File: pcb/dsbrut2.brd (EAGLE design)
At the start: 51.6 x 38 mm, 14 parts, among them IC1 4175D, IC2 74HC125D, IC3 MEGA8-AI

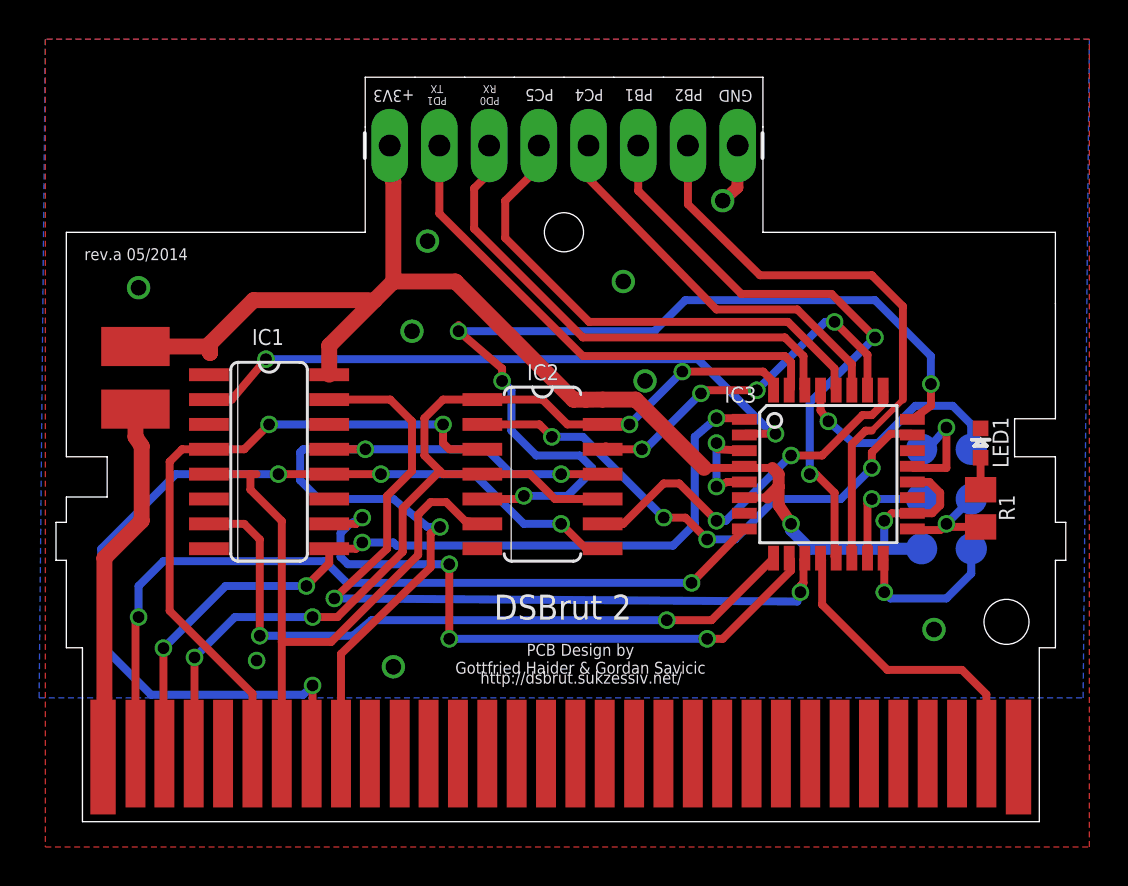
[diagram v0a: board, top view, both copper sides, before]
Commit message: Made pin1 of the ICSP connector square
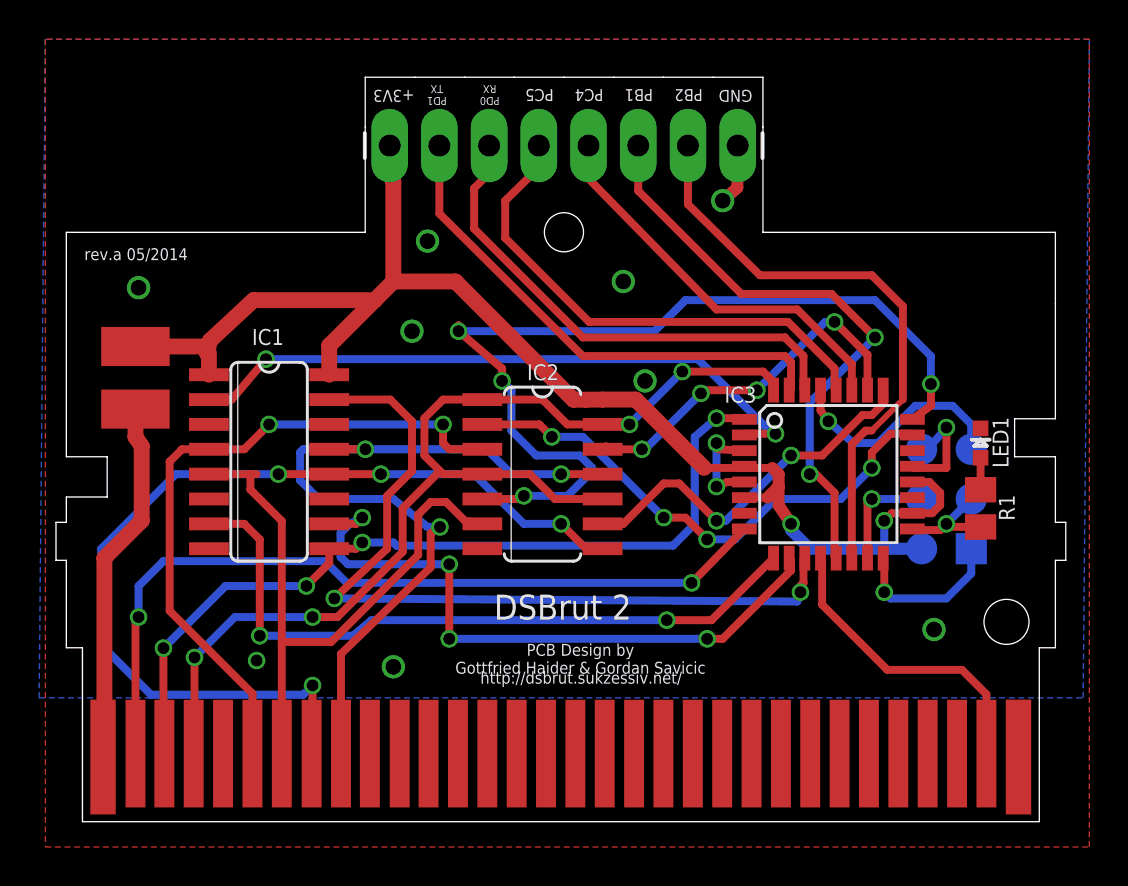
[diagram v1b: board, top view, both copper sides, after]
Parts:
- TP3: value TPSQTP16R -> TPSQTP16SQ; device testpad:TP16R -> testpad:TP16SQ
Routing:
- net +3V3: track 69.8 -> 71.1 mm
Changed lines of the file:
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@@
 <elements>
 <element name="IC1" library="40xx" package="SO16" value="4175D" x="9.525" y="18.415" smashed="yes" rot="R270">
-<attribute name="VALUE" x="8.255" y="17.0815" size="0.8128" layer="27" ratio="10" rot="R270"/>
+<attribute name="VALUE" x="9.525" y="18.3515" size="0.8128" layer="27" ratio="10" rot="R270" align="center"/>
 <attribute name="NAME" x="8.646478125" y="24.380178125" size="0.8128" layer="25" ratio="10"/>
 </element>
 <element name="IC2" library="74xx-eu" package="SO14" value="74HC125D" x="23.495" y="17.78" smashed="yes" rot="R270">
-<attribute name="VALUE" x="28.1305" y="19.05" size="0.8128" layer="27" ratio="10" rot="R270"/>
+<attribute name="VALUE" x="23.0505" y="20.47875" size="0.8128" layer="27" ratio="10" rot="R270" align="center"/>
 <attribute name="NAME" x="22.7028625" y="22.578071875" size="0.8128" layer="25" ratio="10"/>
 </element>
@@
 <attribute name="OC_FARNELL" value="9171371" x="55.88" y="-26.67" size="1.778" layer="27" display="off"/>
 <attribute name="NAME" x="32.7914" y="21.43125" size="0.8128" layer="25"/>
-<attribute name="VALUE" x="37.7825" y="15.0749" size="0.8128" layer="27" rot="R90"/>
+<attribute name="VALUE" x="38.1" y="17.77365" size="0.8128" layer="27" rot="R90" align="center"/>
 </element>
 <element name="U$1" library="nds_cart" package="DS-CARTRIDGE-SLOT2" value="DS_CARTRIDGE_SLOT2" x="0" y="0"/>
 <element name="TP1" library="testpad" package="TP16R" value="TPSQTP16R" x="42.8625" y="13.97" smashed="yes" rot="MR0">
 <attribute name="TP_SIGNAL_NAME" value="" x="42.8625" y="11.43" size="1" layer="38" rot="MR0"/>
-<attribute name="NAME" x="43.6626" y="14.8199" size="0.8128" layer="26" rot="MR0"/>
-<attribute name="VALUE" x="43.4975" y="13.208" size="0.0254" layer="28" rot="MR0"/>
 </element>
 <element name="TP2" library="testpad" package="TP16R" value="TPSQTP16R" x="42.8625" y="16.51" smashed="yes" rot="MR0">
 <attribute name="TP_SIGNAL_NAME" value="" x="42.8625" y="13.97" size="1" layer="38" rot="MR0"/>
-<attribute name="NAME" x="43.6626" y="17.3599" size="0.8128" layer="26" rot="MR0"/>
-<attribute name="VALUE" x="43.4975" y="15.748" size="0.0254" layer="28" rot="MR0"/>
 </element>
-<element name="TP3" library="testpad" package="TP16R" value="TPSQTP16R" x="45.4025" y="13.97" smashed="yes" rot="MR0">
+<element name="TP3" library="testpad" package="TP16SQ" value="TPSQTP16SQ" x="45.4025" y="13.97" smashed="yes" rot="MR0">
 <attribute name="TP_SIGNAL_NAME" value="" x="45.4025" y="11.43" size="1" layer="38" rot="MR0"/>
-<attribute name="NAME" x="46.2026" y="14.8199" size="0.8128" layer="26" rot="MR0"/>
-<attribute name="VALUE" x="46.0375" y="13.208" size="0.0254" layer="28" rot="MR0"/>
 </element>
 <element name="TP4" library="testpad" package="TP16R" value="TPSQTP16R" x="45.4025" y="16.51" smashed="yes" rot="MR0">
 <attribute name="TP_SIGNAL_NAME" value="" x="45.4025" y="13.97" size="1" layer="38" rot="MR0"/>
-<attribute name="NAME" x="46.2026" y="17.3599" size="0.8128" layer="26" rot="MR0"/>
-<attribute name="VALUE" x="46.0375" y="15.748" size="0.0254" layer="28" rot="MR0"/>
 </element>
 <element name="TP5" library="testpad" package="TP16R" value="TPSQTP16R" x="45.4025" y="19.05" smashed="yes" rot="MR0">
 <attribute name="TP_SIGNAL_NAME" value="" x="45.4025" y="16.51" size="1" layer="38" rot="MR0"/>
-<attribute name="NAME" x="46.2026" y="19.8999" size="0.8128" layer="26" rot="MR0"/>
-<attribute name="VALUE" x="46.0375" y="18.288" size="0.0254" layer="28" rot="MR0"/>
 </element>
 <element name="TP6" library="testpad" package="TP16R" value="TPSQTP16R" x="42.8625" y="19.05" smashed="yes" rot="MR0">
 <attribute name="TP_SIGNAL_NAME" value="" x="42.8625" y="16.51" size="1" layer="38" rot="MR0"/>
-<attribute name="NAME" x="43.6626" y="19.8999" size="0.8128" layer="26" rot="MR0"/>
 </element>
 <element name="LED1" library="SparkFunEagle-6-6-07" package="LED-0603" value="" x="45.87875" y="19.3675" smashed="yes">
@@
 <wire x1="43.815" y1="16.8275" x2="43.2625" y2="17.38" width="0.4064" layer="1"/>
 <contactref element="F1" pad="1"/>
-<wire x1="8.73125" y1="26.67" x2="6.50875" y2="24.4475" width="0.8128" layer="1"/>
-<wire x1="6.50875" y1="24.4475" x2="6.50875" y2="23.97125" width="0.8128" layer="1"/>
-<wire x1="6.50875" y1="23.97125" x2="6.50875" y2="22.91715" width="0" layer="19" extent="1-16"/>
-<wire x1="6.50875" y1="22.91715" x2="6.4516" y2="22.86" width="0" layer="19" extent="1-16"/>
+<wire x1="6.50875" y1="24.60625" x2="6.35" y2="23.97125" width="0.8128" layer="1"/>
 <wire x1="2.69875" y1="24.30125" x2="6.3625" y2="24.30125" width="0.8128" layer="1"/>
-<wire x1="6.3625" y1="24.30125" x2="6.50875" y2="23.97125" width="0.8128" layer="1"/>
+<wire x1="6.3625" y1="24.30125" x2="6.35" y2="23.97125" width="0.8128" layer="1"/>
 <contactref element="IC1" pad="16"/>
 <wire x1="12.5984" y1="22.86" x2="12.5984" y2="24.3459" width="0.8128" layer="1"/>
 <wire x1="12.5984" y1="24.3459" x2="14.9225" y2="26.67" width="0.8128" layer="1"/>
+<wire x1="6.35" y1="23.97125" x2="6.4516" y2="23.97125" width="0.4064" layer="1"/>
+<wire x1="6.4516" y1="23.97125" x2="6.4516" y2="22.86" width="0.8128" layer="1"/>
+<wire x1="8.73125" y1="26.67" x2="6.50875" y2="24.60625" width="0.8128" layer="1"/>
 </signal>
 <signal name="PD1">

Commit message: added crystal, jumper bridge for gba2
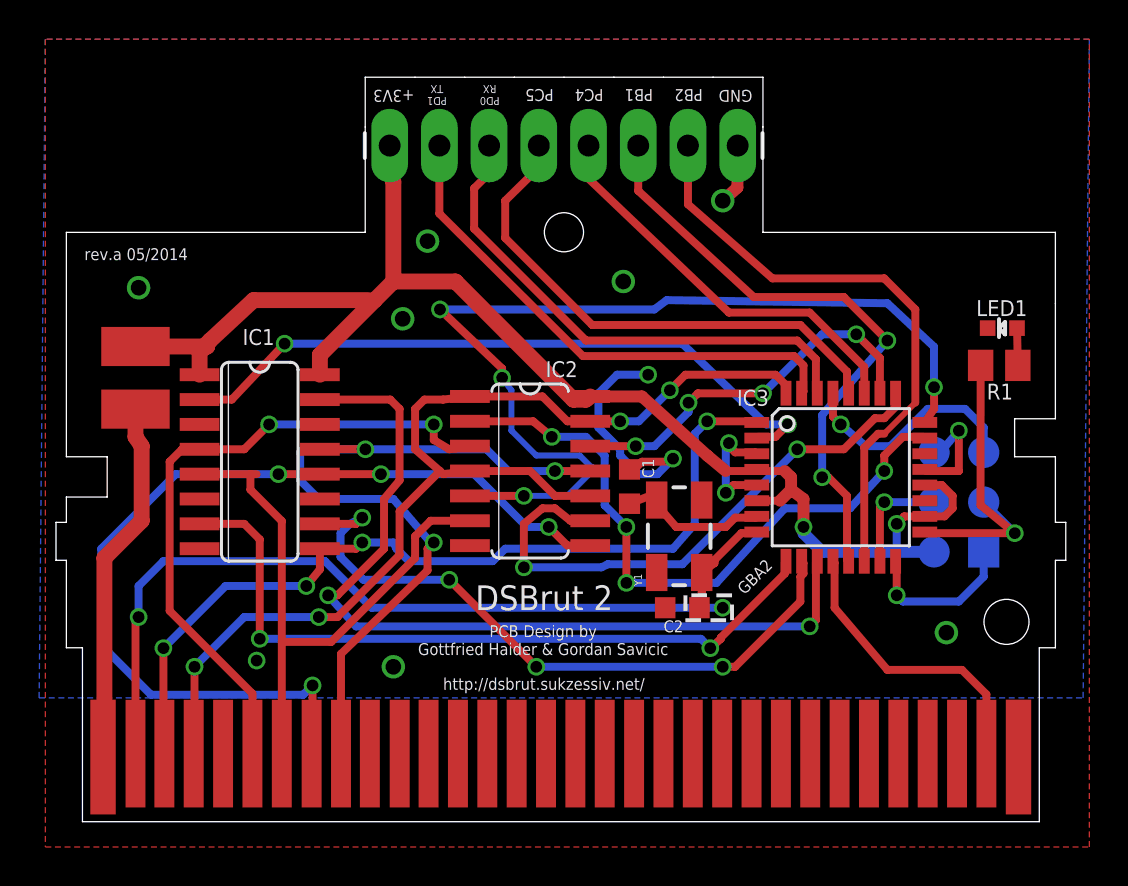
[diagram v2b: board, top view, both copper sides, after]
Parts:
- added C1, C2: (no value), rcl:C0603K
- added Y1: (no value), SparkFun-FreqCtrl:CRYSTAL-SMD-5X3
- moved R1 7.36 mm to (46.8, 23.3), turned to 0 degrees
- moved LED1 5.98 mm to (47.0, 25.2), turned to 90 degrees
- moved TP1 0.65 mm to (43.5, 13.8)
- moved TP2 0.65 mm to (43.5, 16.4)
- moved TP6 0.65 mm to (43.5, 18.9)
- moved IC2 0.65 mm to (22.9, 17.9)
- moved IC3 0.65 mm to (38.7, 17.6)
- moved TP3 0.65 mm to (46.0, 13.8)
- moved TP4 0.65 mm to (46.0, 16.4)
- moved TP5 0.65 mm to (46.0, 18.9)
- moved IC1 0.48 mm to (9.05, 18.4)
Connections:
- new net N$3: C1.2, IC3.7, Y1.3
- new net PB7: C2.2, IC3.8, Y1.1
- net GBA2: no longer IC3.8
- net GND: now also C1.1, C2.1
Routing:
- net GND: track 14.1 -> 26.9 mm, vias 12 -> 13
- net SCK: track 5.64 -> 16.3 mm
- net PC2: track 19.2 -> 29.2 mm
- net N$3: track 0.00 -> 7.81 mm
- net PC0: track 27.1 -> 33.5 mm
- net PB7: track 0.00 -> 5.53 mm
- net PD7: track 41.4 -> 44.3 mm
- net PC1: track 47.6 -> 49.9 mm
- net PD5: track 35.7 -> 37.8 mm
- net GBA2: track 41.7 -> 40.0 mm
- net PD4: track 33.1 -> 34.8 mm
- net WR: track 43.1 -> 44.8 mm
- net PC3: track 19.0 -> 20.5 mm
- net GBA7: track 32.2 -> 30.7 mm
- net +3V3: track 71.1 -> 72.2 mm
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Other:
- board text added: "GBA2"

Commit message: cleanup, added our two faces on silkscreen layer
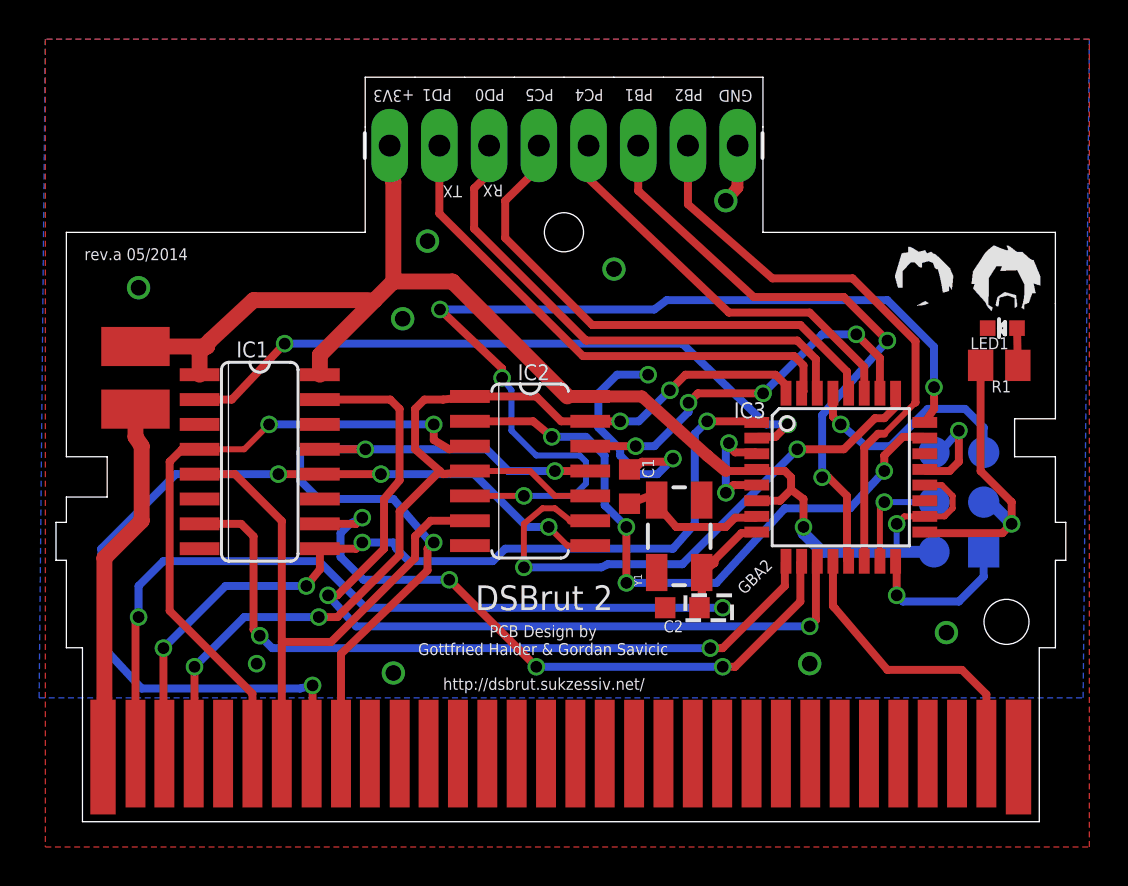
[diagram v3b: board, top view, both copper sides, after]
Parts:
- C1, C2: value (none) -> 10pf
- R1: value (none) -> 220r
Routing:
- net SCK: track 16.3 -> 15.3 mm
- net PB2: track 30.8 -> 29.9 mm
- net GBA7: track 30.7 -> 29.9 mm
- net GND: track 26.9 -> 26.5 mm, vias 13 -> 14
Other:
- board text added: "PD0"
- board text added: "PD1"
- board text added: "RX"
- board text added: "TX"
- board text removed: "PD0 RX"
- board text removed: "PD1 TX"

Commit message: added c3 between vcc and gnd, moved c2 away from steg
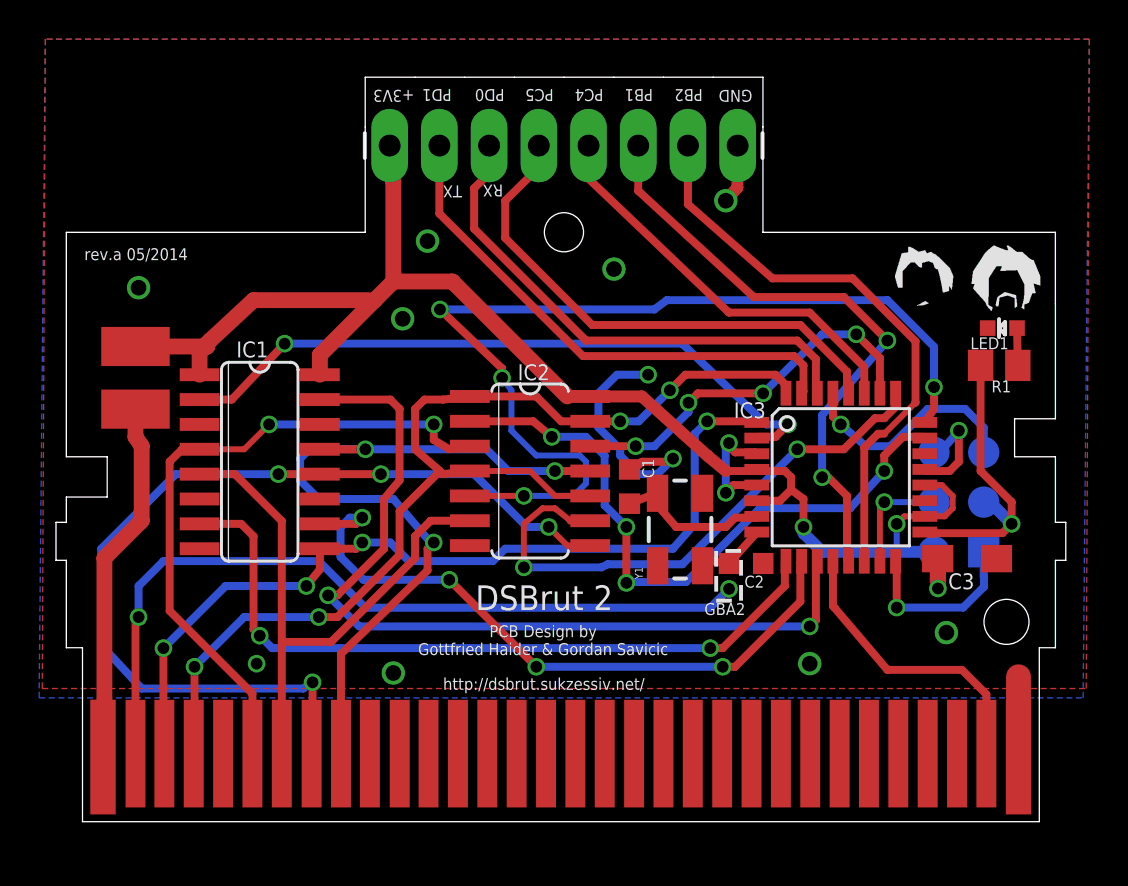
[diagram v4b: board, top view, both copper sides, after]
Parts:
- added C3: (no value), rcl:SMC_A
- moved C2 3.97 mm to (33.9, 13.2), turned to 180 degrees
- moved Y1 0.35 mm to (30.5, 15.0)
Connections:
- net +3V3: now also C3.+
- net GND: now also C3.-
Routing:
- net GND: track 26.5 -> 30.7 mm
- net +3V3: track 72.1 -> 75.6 mm, vias 2 -> 3
- net PB7: track 5.53 -> 3.89 mm
- net MISO: track 8.14 -> 9.08 mm
- net GBA2: track 40.0 -> 40.7 mm
